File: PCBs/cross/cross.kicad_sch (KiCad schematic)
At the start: 13 parts, among them J2 Conn_01x04, U1 ctrlr_TL, U2 LEDs_T, U3 ctrlr_BR, U4 LEDs_B, U5 LEDs_R, U6 LEDs_L, U7 ctrlr_C, U9 LEDs_C

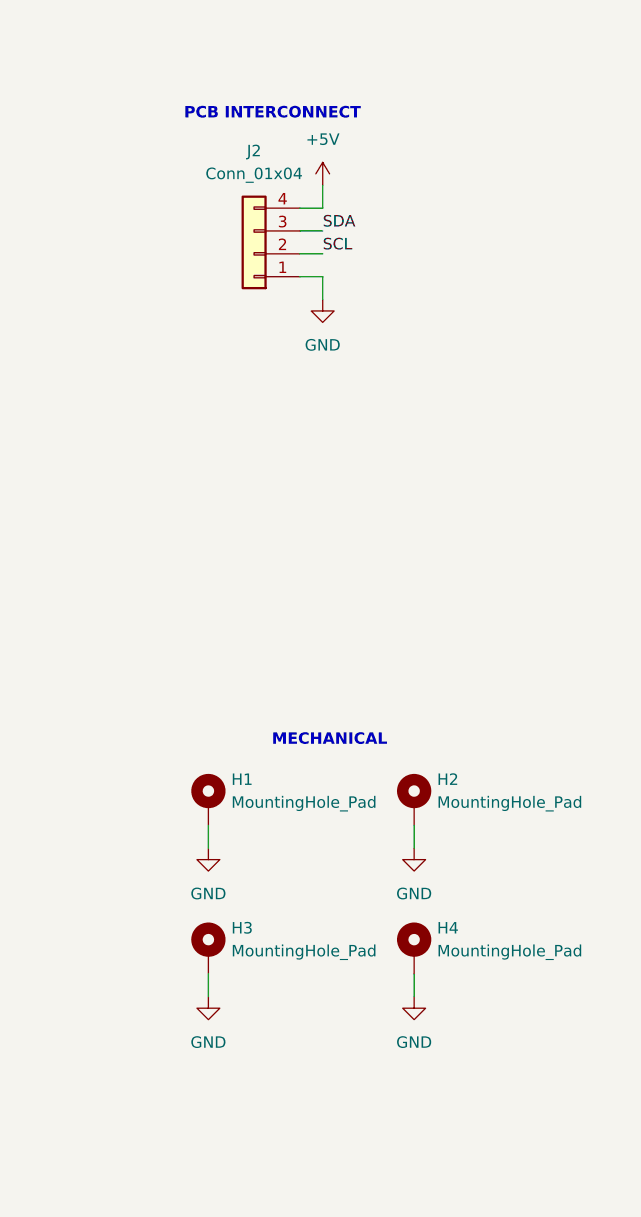
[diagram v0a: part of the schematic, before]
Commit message: Cross routing 1/3 done
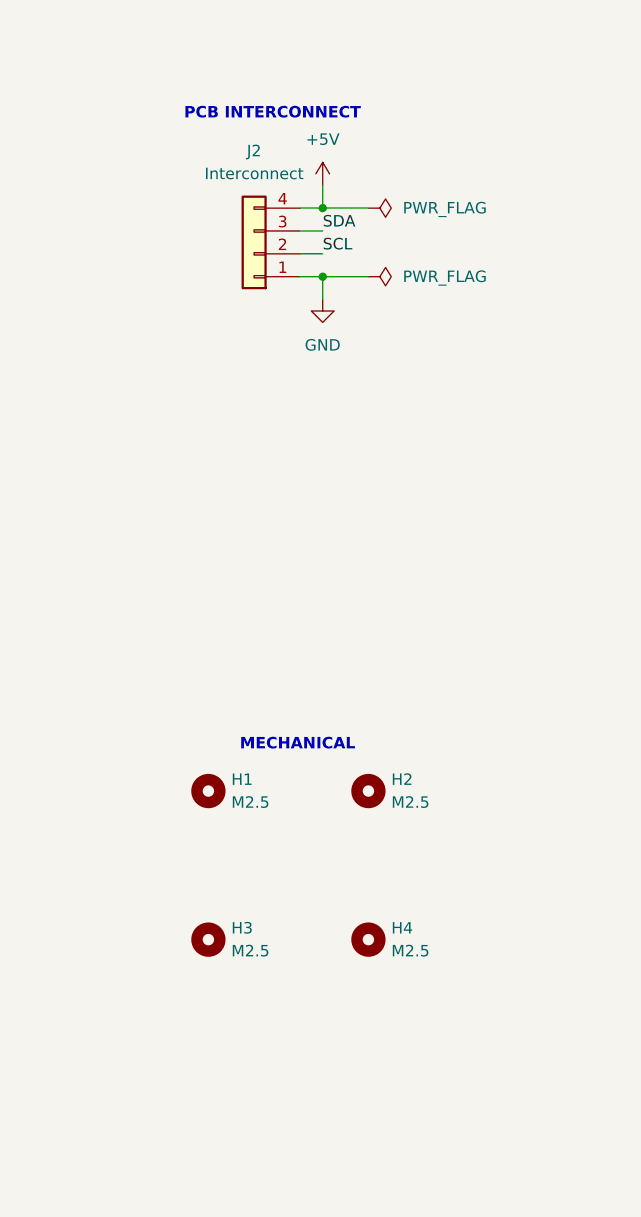
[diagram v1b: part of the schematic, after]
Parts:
- removed H1, H2, H3, H4: MountingHole_Pad, MountingHole:MountingHole_2.7mm_M2.5_ISO7380_Pad, symbol Mechanical:MountingHole_Pad
- added H1, H2, H3, H4: M2.5, MountingHole:MountingHole_2.7mm_M2.5, symbol Mechanical:MountingHole
- J2: value Conn_01x04 -> Interconnect

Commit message: Finished PCBs, ready to order
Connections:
- net at U1.6 (C4), U2.1 (C4): now also U5.1 (C4); no longer U6.1 (C4)
- net at U6.10 (A3): now also U3.22 (A3); no longer U1.14 (A11)
- net at U6.11 (A5): now also U3.20 (A5); no longer U1.12 (A13)
- net at U1.5 (C3), U2.12 (C3): now also U5.12 (C3); no longer U6.12 (C3)
- net at U6.13 (A0): now also U3.25 (A0); no longer U1.17 (A8)
- net at U1.3 (C1), U2.14 (C1): now also U5.14 (C1); no longer U6.14 (C1)
- net at U6.15 (A6): now also U3.19 (A6); no longer U1.11 (A14)
- net at U6.16 (A7): now also U3.18 (A7); no longer U1.10 (A15)
- net at U1.8 (C6), U2.2 (C6): now also U5.2 (C6); no longer U6.2 (C6)
- net at U6.3 (A1): now also U3.24 (A1); no longer U1.16 (A9)
- net at U6.4 (A2): now also U3.23 (A2); no longer U1.15 (A10)
- net at U1.9 (C7), U2.5 (C7): now also U5.5 (C7); no longer U6.5 (C7)
- net at U6.6 (A4): now also U3.21 (A4); no longer U1.13 (A12)
- net at U1.7 (C5), U2.7 (C5): now also U5.7 (C5); no longer U6.7 (C5)
- net at U1.4 (C2), U2.8 (C2): now also U5.8 (C2); no longer U6.8 (C2)
- net at U1.2 (C0), U2.9 (C0): now also U5.9 (C0); no longer U6.9 (C0)
- net at U3.6 (C4), U4.1 (C4): now also U6.1 (C4); no longer U5.1 (C4)
- net at U5.10 (A3): now also U1.14 (A11); no longer U3.22 (A3)
- net at U5.11 (A5): now also U1.12 (A13); no longer U3.20 (A5)
- net at U3.5 (C3), U4.12 (C3): now also U6.12 (C3); no longer U5.12 (C3)
- net at U5.13 (A0): now also U1.17 (A8); no longer U3.25 (A0)
- net at U3.3 (C1), U4.14 (C1): now also U6.14 (C1); no longer U5.14 (C1)
- net at U5.15 (A6): now also U1.11 (A14); no longer U3.19 (A6)
- net at U5.16 (A7): now also U1.10 (A15); no longer U3.18 (A7)
- net at U3.8 (C6), U4.2 (C6): now also U6.2 (C6); no longer U5.2 (C6)
- net at U5.3 (A1): now also U1.16 (A9); no longer U3.24 (A1)
- net at U5.4 (A2): now also U1.15 (A10); no longer U3.23 (A2)
- net at U3.9 (C7), U4.5 (C7): now also U6.5 (C7); no longer U5.5 (C7)
- net at U5.6 (A4): now also U1.13 (A12); no longer U3.21 (A4)
- net at U3.7 (C5), U4.7 (C5): now also U6.7 (C5); no longer U5.7 (C5)
- net at U3.4 (C2), U4.8 (C2): now also U6.8 (C2); no longer U5.8 (C2)
- net at U3.2 (C0), U4.9 (C0): now also U6.9 (C0); no longer U5.9 (C0)
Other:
- moved on the sheet: U5, U6
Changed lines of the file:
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@@
 	(symbol
 		(lib_id "parts_library:KWM-30881APGB")
-		(at 69.85 55.88 0)
+		(at 95.25 121.92 0)
 		(unit 1)
 		(exclude_from_sim no)
@@
 		(fields_autoplaced yes)
 		(property "Reference" "U6"
-			(at 85.09 55.2449 0)
+			(at 110.49 121.2849 0)
 			(effects
 				(font
@@
 		)
 		(property "Value" "LEDs_L"
-			(at 85.09 57.15 0)
+			(at 110.49 123.19 0)
 			(effects
 				(font
@@
 		)
 		(property "Footprint" "lib_pharmacy:KWM-30881"
-			(at 69.85 55.88 0)
+			(at 95.25 121.92 0)
 			(effects
 				(font
@@
 		)
 		(property "Datasheet" ""
-			(at 69.85 55.88 0)
+			(at 95.25 121.92 0)
 			(effects
 				(font
@@
 		)
 		(property "Description" ""
-			(at 69.85 55.88 0)
+			(at 95.25 121.92 0)
 			(effects
 				(font
@@
 	(symbol
 		(lib_id "parts_library:KWM-30881APGB")
-		(at 95.25 121.92 0)
+		(at 69.85 55.88 0)
 		(unit 1)
 		(exclude_from_sim no)
@@
 		(fields_autoplaced yes)
 		(property "Reference" "U5"
-			(at 110.49 121.2849 0)
+			(at 85.09 55.2449 0)
 			(effects
 				(font
@@
 		)
 		(property "Value" "LEDs_R"
-			(at 110.49 123.19 0)
+			(at 85.09 57.15 0)
 			(effects
 				(font
@@
 		)
 		(property "Footprint" "lib_pharmacy:KWM-30881"
-			(at 95.25 121.92 0)
+			(at 69.85 55.88 0)
 			(effects
 				(font
@@
 		)
 		(property "Datasheet" ""
-			(at 95.25 121.92 0)
+			(at 69.85 55.88 0)
 			(effects
 				(font
@@
 		)
 		(property "Description" ""
-			(at 95.25 121.92 0)
-			(effects
-				(font
+			(at 69.85 55.88 0)
+			(effects
+				(font
